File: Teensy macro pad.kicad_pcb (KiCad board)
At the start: 2 copper layers, 79 x 122.4 mm, 52 parts, among them J1 USB_C_Receptacle_USB2.0_14P, J2 AVR-ISP-6, J3 Conn_01x05_Pin, SW0,0 CherryMX, SW0,1 CherryMX, SW0,2 CherryMX, SW0,3 CherryMX, SW0,4 CherryMX, SW1 SW_Push, SW1,0 CherryMX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

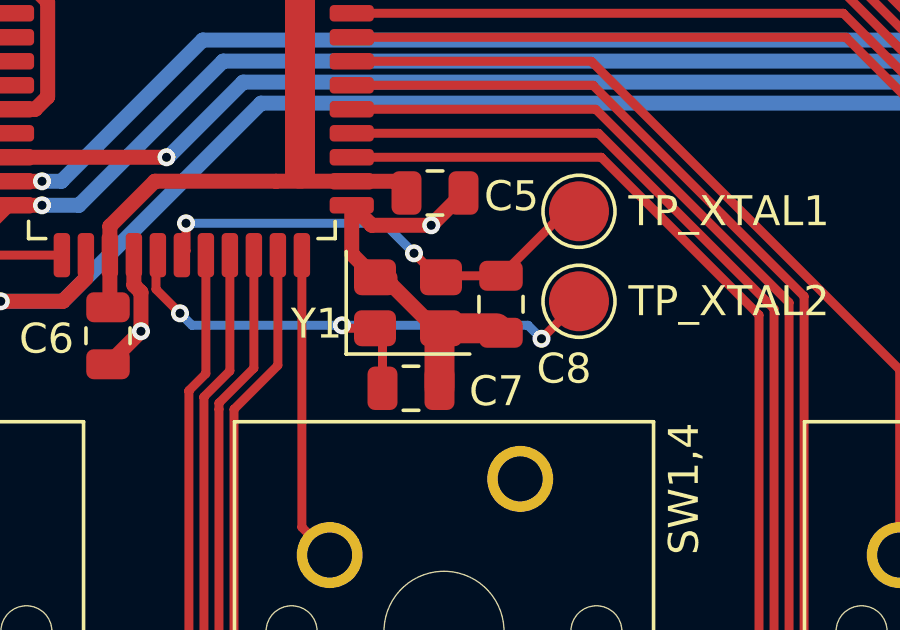
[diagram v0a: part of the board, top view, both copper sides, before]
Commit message: Add JLCPCB part numbers
C7 and C8 (10pF capacitors) had to be changed to a smaller 0603
footprint, so that I could use parts on the basic JLCPCB parts list.
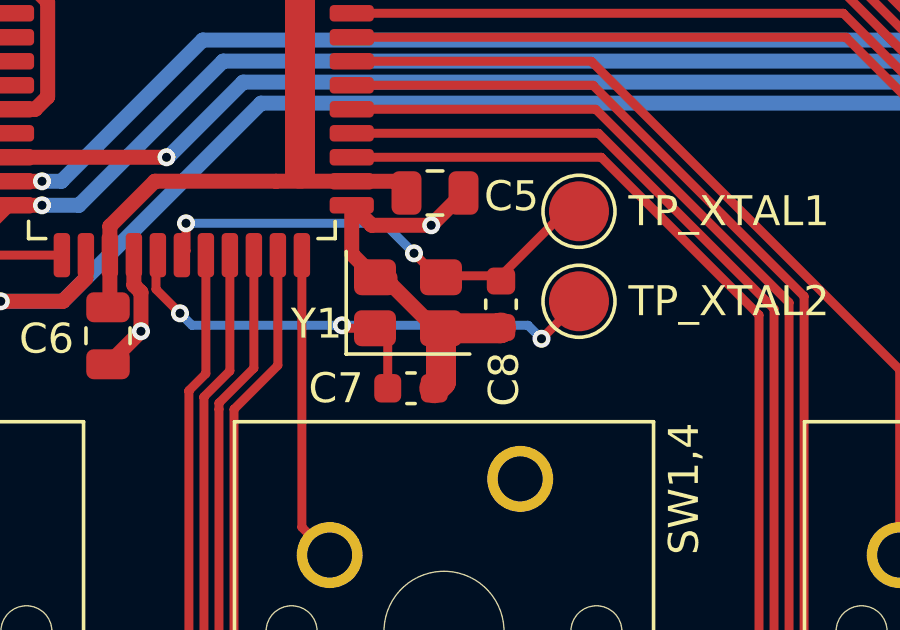
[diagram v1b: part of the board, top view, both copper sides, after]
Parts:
- C7, C8: footprint Capacitor_SMD:C_0805_2012Metric -> Capacitor_SMD:C_0603_1608Metric

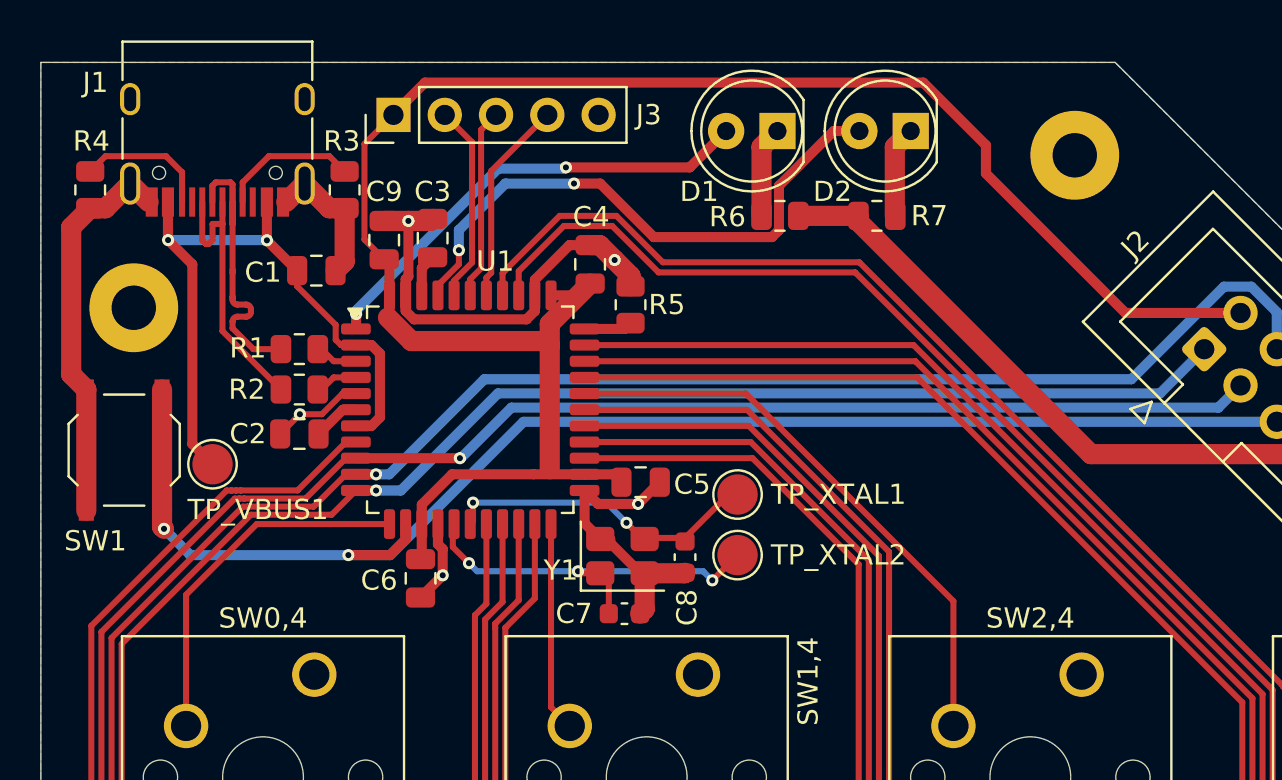
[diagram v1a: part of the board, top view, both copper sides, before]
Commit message: Add labels and improve silkscreens
Capacitors and resistors now follow the rule that their silkscreen label
should be in the same orientation as the component. Also added labels
for pin headers, and a copyright notice and GitHub link to the back.
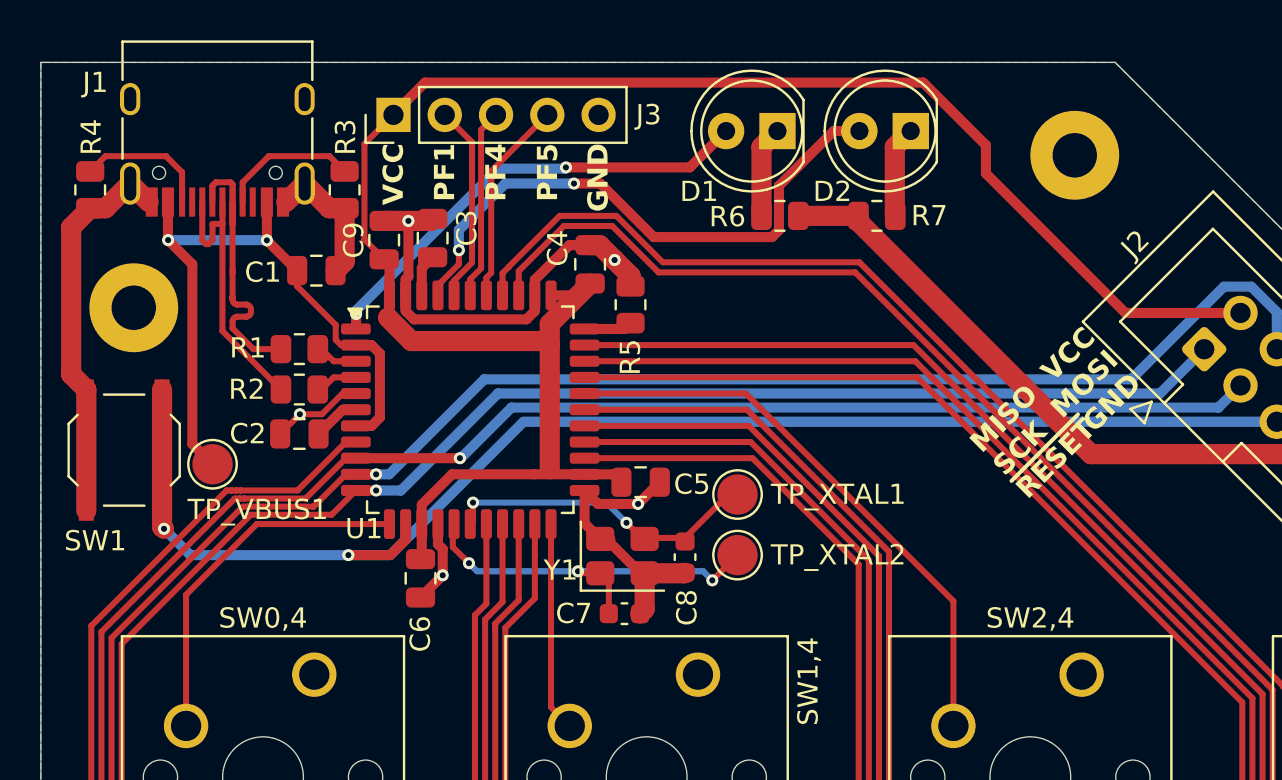
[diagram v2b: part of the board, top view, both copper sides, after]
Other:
- board text added: "GND"
- board text added: "MISO SCK ~{RESET}"
- board text added: "PF1"
- board text added: "PF4"
- board text added: "PF5"
- board text added: "VCC"
- board text added: "VCC MOSI GND"
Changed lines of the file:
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@@
 			(at 5 1.5 0)
 			(layer "F.Fab")
+			(hide yes)
 			(effects
 				(font
@@
 		(tags "capacitor")
 		(property "Reference" "C4"
-			(at 2.35 0.05 180)
+			(at 0.8 -1.6 270)
 			(layer "F.SilkS")
 			(effects
@@
 		)
 		(property "Value" "0.1uF"
-			(at 0 1.68 90)
+			(at 1.8 1.7 90)
 			(layer "F.Fab")
 			(effects
@@
 		(tags "resistor")
 		(property "Reference" "R3"
-			(at -2.4125 0.14175 0)
+			(at -2.6125 -0.05825 90)
 			(layer "F.SilkS")
 			(effects
@@
 		)
 		(property "Value" "1uF"
-			(at 0 1.68 0)
+			(at 0.45825 1.68 0)
 			(layer "F.Fab")
 			(effects
@@
 		)
 		(property "Value" "22"
-			(at -0.05 -1.8 0)
+			(at -0.9 -1.5 0)
 			(layer "F.Fab")
 			(effects
@@
 		(tags "capacitor")
 		(property "Reference" "C9"
-			(at 2.4 0 180)
+			(at 0 -1.5 270)
 			(layer "F.SilkS")
 			(effects
@@
 		)
 		(property "Value" "0.1uF"
-			(at 0 1.68 90)
+			(at 0 1.2 90)
 			(layer "F.Fab")
 			(effects
@@
 		(tags "capacitor")
 		(property "Reference" "C3"
-			(at -2.3 0 0)
+			(at -0.5 -1.7 90)
 			(layer "F.SilkS")
 			(effects
@@
 		)
 		(property "Value" "0.1uF"
-			(at 0 1.68 90)
+			(at -0.5 -3 90)
 			(layer "F.Fab")
 			(effects
@@
 		(tags "resistor")
 		(property "Reference" "R4"
-			(at -2.4125 -0.05825 0)
+			(at -2.6125 -0.05825 90)
 			(layer "F.SilkS")
 			(effects
@@
 		(tags "resistor")
 		(property "Reference" "R5"
-			(at 0 1.8 180)
+			(at -2.6 0 270)
 			(layer "F.SilkS")
 			(effects
@@
 		)
 		(property "Value" "1K"
-			(at 0 3.3 90)
+			(at 0 1.9 90)
 			(layer "F.Fab")
 			(effects
@@
 		)
 		(property "Value" "16 MHz"
-			(at 5.2 -2.45 0)
+			(at 0.7 -1.95 0)
 			(layer "F.Fab")
 			(effects
@@
 		)
 		(property "Value" "0.1uF"
-			(at 0 1.68 0)
+			(at 0.5 -1.59 0)
 			(layer "F.Fab")
 			(effects
@@
 		(tags "TQFP QFP")
 		(property "Reference" "U1"
-			(at 1.2375 -7.35 0)
+			(at -5.2625 5.9 0)
 			(layer "F.SilkS")
 			(effects
@@
 		)
 		(property "Value" "ATmega32U4-A"
-			(at -1.6625 7.6 0)
+			(at -3.3625 7.6 0)
 			(layer "F.Fab")
 			(effects
@@
 			(at 2 3.75 0)
 			(layer "F.Fab")
+			(hide yes)
 			(effects
 				(font
@@
 		(tags "capacitor")
 		(property "Reference" "C6"
-			(at 0.1 2.05 0)
+			(at 2.75 0 90)
 			(layer "F.SilkS")
 			(effects
@@
 		)
 		(property "Value" "0.1uF"
-			(at 3.85 -0.2 90)
+			(at 2.75 -1.3 90)
 			(layer "F.Fab")
 			(effects
@@
 			(at 5 1.5 0)
 			(layer "F.Fab")
+			(hide yes)
 			(effects
 				(font
@@
 		(layer "Edge.Cuts")
 	)
+	(gr_text "VCC"
+		(at 53.46 35.6 90)
+		(layer "F.SilkS")
+		(effects
+			(font
+				(size 1 1)
+				(thickness 0.2)
+				(bold yes)
+			)
+			(justify right)
+		)
+	)
+	(gr_text "MISO\nSCK\n~{RESET}"
+		(at 83.4 51.8 45)
+		(layer "F.SilkS")
+		(effects
+			(font
+				(size 1 1)
+				(thickness 0.2)
+				(bold yes)
+			)
+			(justify left)
+		)
+	)
+	(gr_text "VCC\nMOSI\nGND"
+		(at 89.1 46.1 45)
+		(layer "F.SilkS")
+		(effects
+			(font
+				(size 1 1)
+				(thickness 0.2)
+				(bold yes)
+			)
+			(justify right)
+		)
+	)
+	(gr_text "PF1"
+		(at 56 35.6 90)
+		(layer "F.SilkS")
+		(effects
+			(font
+				(size 1 1)
+				(thickness 0.2)
+				(bold yes)
+			)
+			(justify right)
+		)
+	)
+	(gr_text "PF5"
+		(at 61.1 35.6 90)
+		(layer "F.SilkS")
+		(effects
+			(font
+				(size 1 1)
+				(thickness 0.2)
+				(bold yes)
+			)
+			(justify right)
+		)
+	)
+	(gr_text "GND"
+		(at 63.6 35.6 90)
+		(layer "F.SilkS")
+		(effects
+			(font
+				(size 1 1)
+				(thickness 0.2)
+				(bold yes)
+			)
+			(justify right)
+		)
+	)
+	(gr_text "PF4"
+		(at 58.54 35.6 90)
+		(layer "F.SilkS")
+		(effects
+			(font
+				(size 1 1)
+				(thickness 0.2)
+				(bold yes)
+			)
+			(justify right)
+		)
+	)
+	(gr_text_box "© Harry Cutts 2025\ngithub.com/HarryCutts/number-pad"
+		(start 43.2 39)
+		(end 92.3 57.5)
+		(margins 1.0025 1.0025 1.0025 1.0025)
+		(layer "B.SilkS")
+		(effects
+			(font
+				(size 1.5 1.5)
+				(thickness 0.1875)
+			)
+			(justify left mirror)
+		)
+		(border no)
+		(stroke
+			(width 0)
+			(type dot)
+		)
+	)
 	(segment

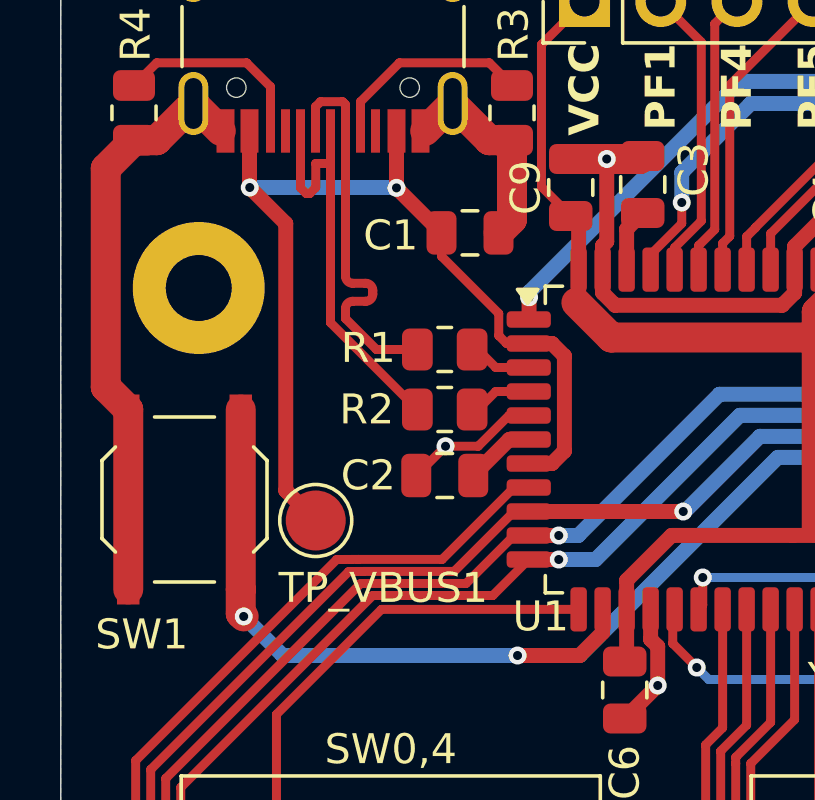
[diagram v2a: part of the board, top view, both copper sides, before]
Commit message: Add USB test points
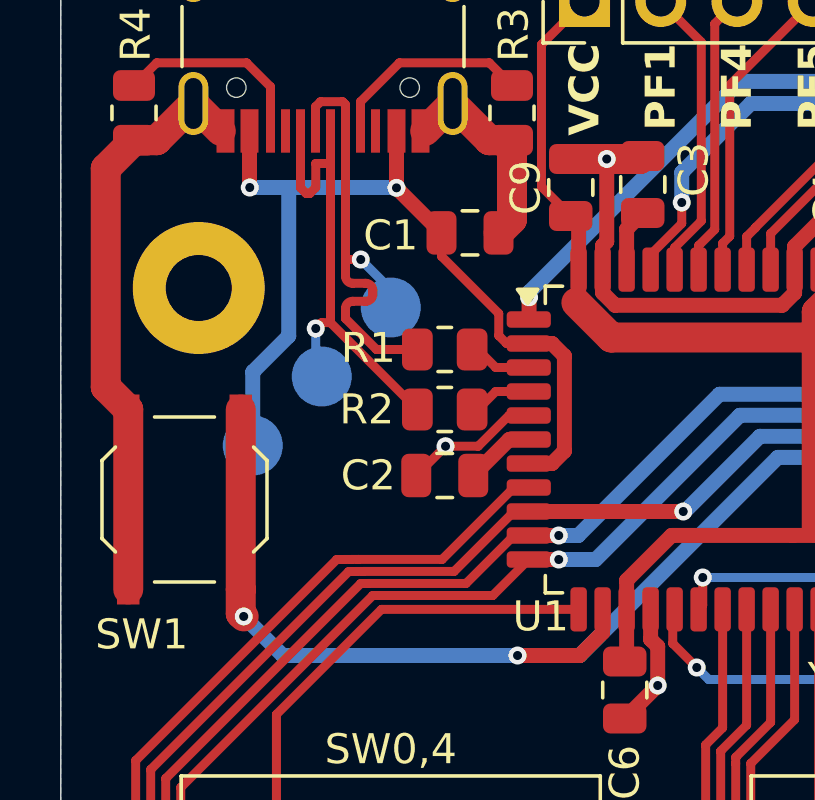
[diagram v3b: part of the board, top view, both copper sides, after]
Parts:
- added TP_D+1: TestPoint, TestPoint:TestPoint_Pad_D2.0mm, B.Cu at (44.7, 46.7)
- added TP_D-1: TestPoint, TestPoint:TestPoint_Pad_D2.0mm, B.Cu at (47.0, 44.4)
- TP_VBUS1: moved to B.Cu
- moved TP_VBUS1 3.26 mm to (42.4, 49.0), turned to 180 degrees
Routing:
- net /VBUS: track 34.0 -> 31.1 mm
- net /J1-D-: track 14.3 -> 16.8 mm, vias 0 -> 1
- net /J1-D+: track 14.3 -> 16.6 mm, vias 0 -> 1

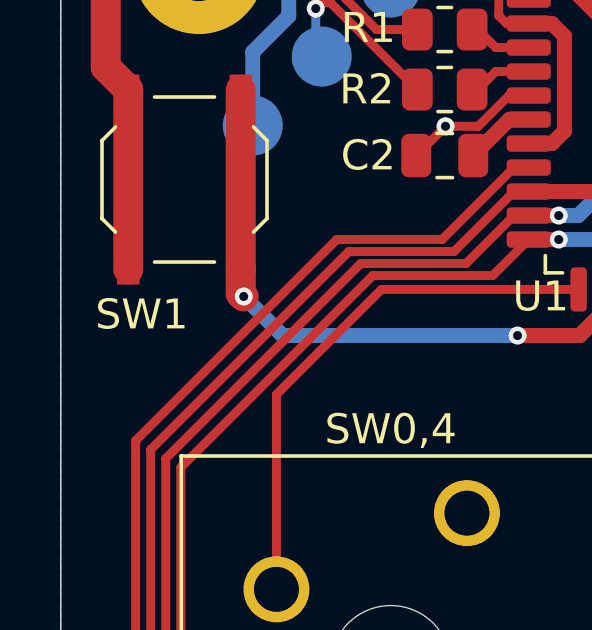
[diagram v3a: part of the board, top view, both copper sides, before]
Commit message: Rename reset switch symbol
Having a switch with reference SW1 as well as ones with SW1,0 to SW1,4
seemed to confuse Fabrication Toolkit or JLCPCB's BOM processor.
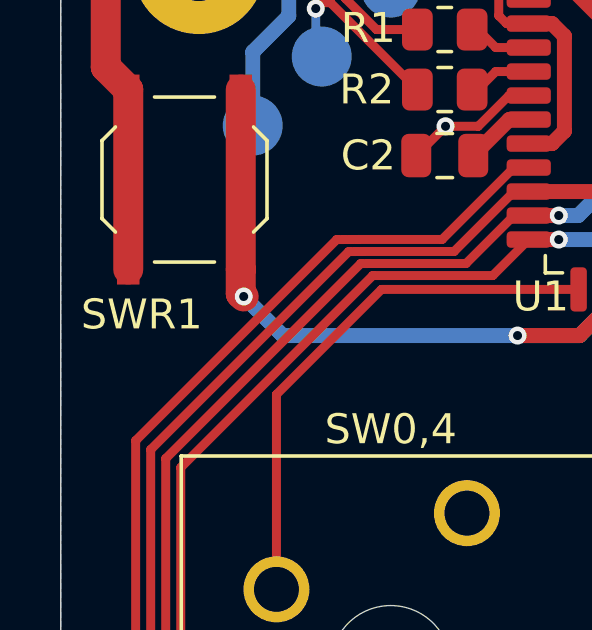
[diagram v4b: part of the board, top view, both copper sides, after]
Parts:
- renumbered SW1 to SWR1
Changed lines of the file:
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@@
 		(descr "SMD Tactile Switch, http://www.helloxkb.com/public/images/pdf/TS-1187A-X-X-X.pdf")
 		(tags "SPST Tactile Switch")
-		(property "Reference" "SW1"
+		(property "Reference" "SWR1"
 			(at -4.5 -1.425 180)
 			(layer "F.SilkS")
